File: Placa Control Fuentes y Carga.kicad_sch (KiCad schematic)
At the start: 139 parts, among them J1 TBP01R1-508-02BE, J10 TBP01R1-508-03BE, J2 TBP01R1-508-02BE, J3 TBP01R1-508-02BE, J4 TBP01R1-508-02BE, J5 TBP01R1-508-02BE, J6 TBP01R1-508-02BE, J7 TBP01R1-508-02BE, J8 TBP01R1-508-02BE, J9 TBP01R1-508-02BE, Q1 IRF9540N, Q2 2N3904, Q3 BC558, Q4 BC558, Q5 IRF5305, Q6 BC337, Q7 BC327, U1 ACS724LLCTR-05AB-T, U2 Relay_Module_WB-083, U3 4N35, U4 LM2596S_Modulo_Regulable, U5 Arduino_Nano_ATmega328P, U6 ACS724LLCTR-05AB-T, U7 MAX485E, U8 MAX22445FAWE+, U9 RI3-0505S

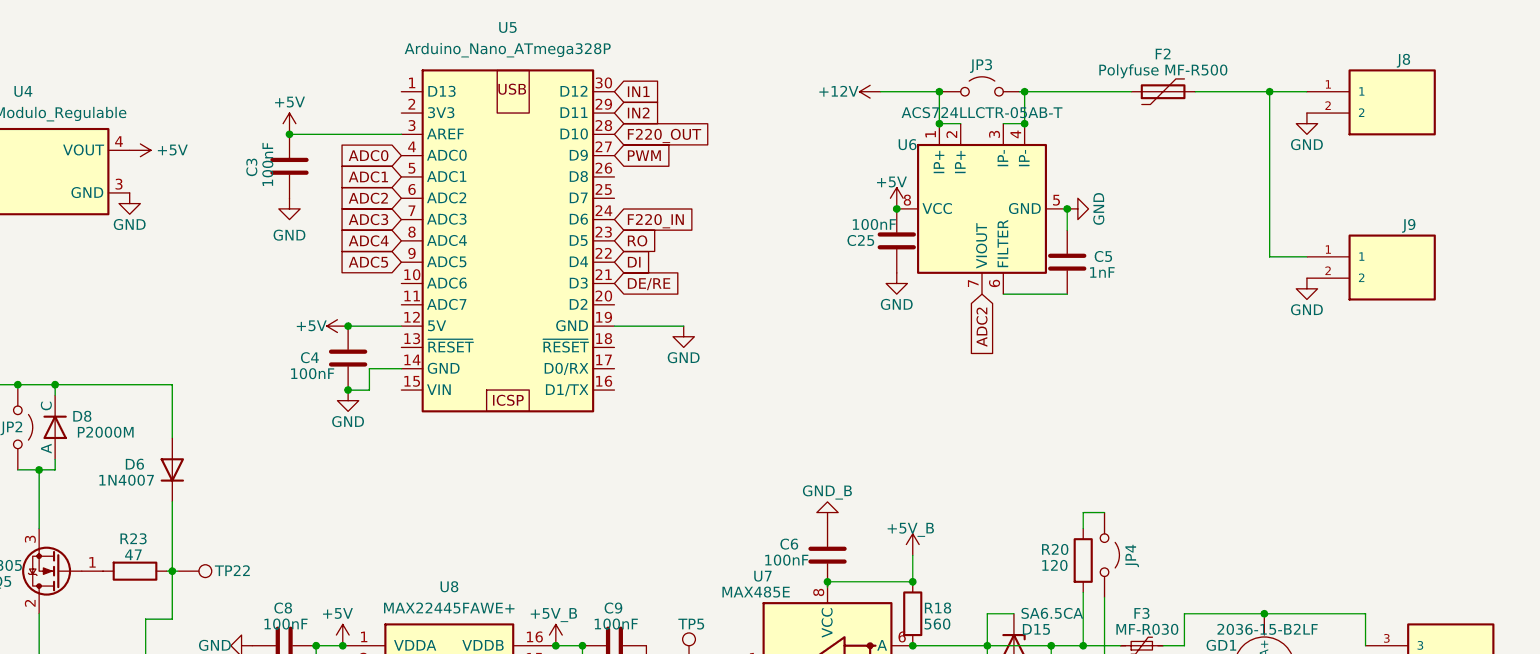
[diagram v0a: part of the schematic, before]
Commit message: Se le agregó el conector con las señales de +5V, GND, ADC0 y apagadoTX para la plaqueita adicional de corte de TX que irá apilada encima con dos tornillos de 1/8 para sujeción mecánica arriba del arduino nano. Se hicieron los gerbers files, se agregó el conecto a la lista de materiales y se le envió a "compras" para su fabricación. Ya se dá por finalizada una primer etapa del proyecto.
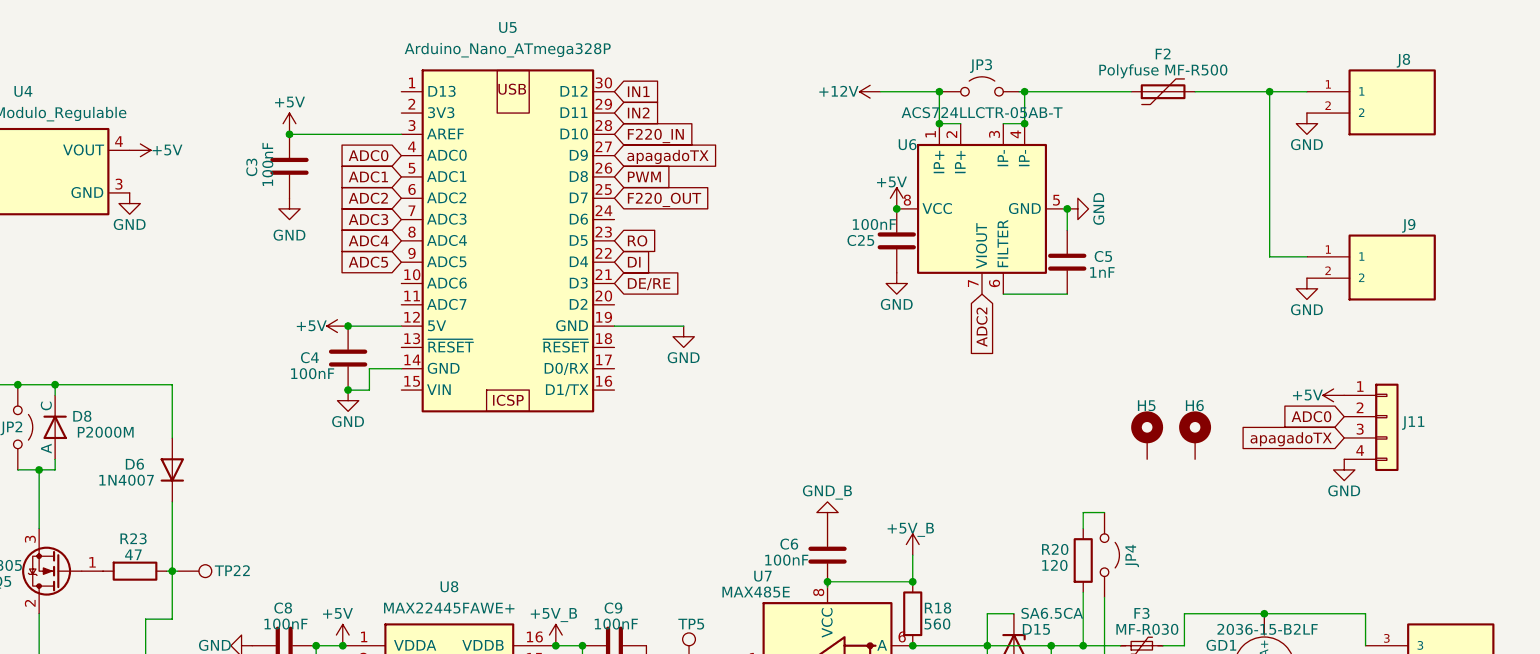
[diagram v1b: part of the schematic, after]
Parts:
- added H5, H6: MountingHole_Pad, MountingHole:MountingHole_3.2mm_M3_Pad, symbol Mechanical:MountingHole_Pad
- added J11: Conn_01x04, Connector_PinHeader_2.54mm:PinHeader_1x04_P2.54mm_Vertical, symbol Connector_Generic:Conn_01x04
- H1, H2, H3, H4: now in the parts list
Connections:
- net +5V: now also J11.1 (Pin_1)
- net ADC0: now also J11.2 (Pin_2)
- net F220_IN: now also U5.28 (D10); no longer U5.24 (D6)
- net F220_OUT: now also U5.25 (D7); no longer U5.28 (D10)
- net GND: now also J11.4 (Pin_4)
- net PWM: now also U5.26 (D8); no longer U5.27 (D9)
- new net apagadoTX: J11.3 (Pin_3), U5.27 (D9)
